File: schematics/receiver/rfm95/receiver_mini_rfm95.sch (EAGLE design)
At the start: 23 parts, among them IC1 ATMEGA328P, Q1 16MHz, Q2 BC817-16SMD, U1 RFM95_LORA_MODULE, U2 AMS1117_3.3

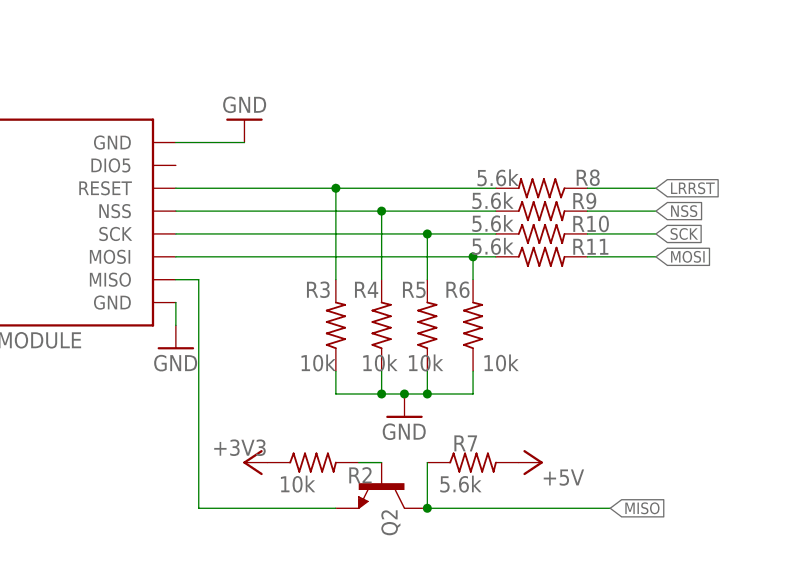
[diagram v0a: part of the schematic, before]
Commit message: Fixed incorrect resistor values
- Fixed incorrect resistor values in the level shifters.
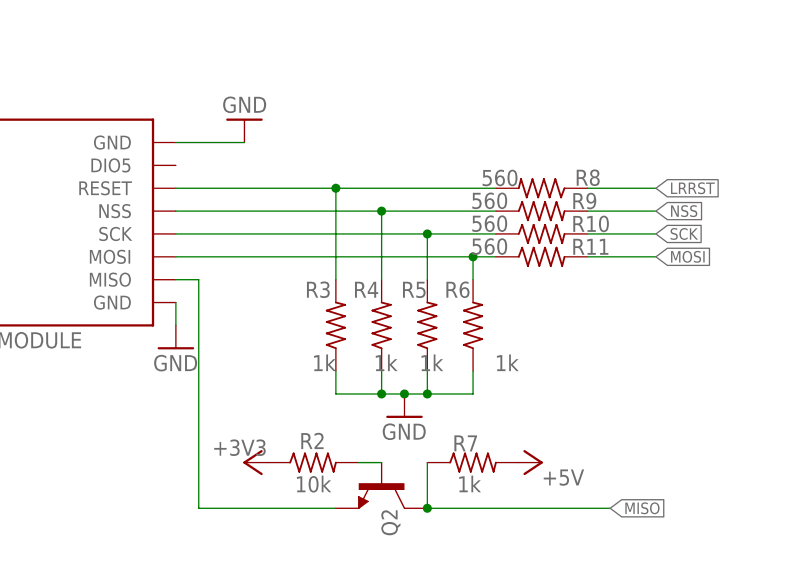
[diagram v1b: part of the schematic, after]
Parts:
- R10, R11, R8, R9: value 5.6k -> 560
- R3, R4, R5, R6: value 10k -> 1k
- R7: value 5.6k -> 1k
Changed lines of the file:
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@@
 <part name="U1" library="RFM95_Lora_module" deviceset="RFM95_LORA_MODULE" device=""/>
 <part name="Q2" library="transistor-npn" deviceset="BC817*" device="SMD" technology="-16" value=""/>
-<part name="R7" library="rcl" deviceset="R-US_" device="R0805" value="5.6k"/>
+<part name="R7" library="rcl" deviceset="R-US_" device="R0805" value="1k"/>
 <part name="R2" library="rcl" deviceset="R-US_" device="R0805" value="10k"/>
 <part name="+3V32" library="supply1" deviceset="+3V3" device=""/>
@@
 <part name="R12" library="rcl" deviceset="R-US_" device="R0805" value="1k"/>
 <part name="P+4" library="supply1" deviceset="+5V" device=""/>
-<part name="R9" library="rcl" deviceset="R-US_" device="R0805" value="5.6k"/>
-<part name="R5" library="rcl" deviceset="R-US_" device="R0805" value="10k"/>
-<part name="R8" library="rcl" deviceset="R-US_" device="R0805" value="5.6k"/>
-<part name="R4" library="rcl" deviceset="R-US_" device="R0805" value="10k"/>
-<part name="R10" library="rcl" deviceset="R-US_" device="R0805" value="5.6k"/>
-<part name="R3" library="rcl" deviceset="R-US_" device="R0805" value="10k"/>
-<part name="R11" library="rcl" deviceset="R-US_" device="R0805" value="5.6k"/>
-<part name="R6" library="rcl" deviceset="R-US_" device="R0805" value="10k"/>
+<part name="R9" library="rcl" deviceset="R-US_" device="R0805" value="560"/>
+<part name="R5" library="rcl" deviceset="R-US_" device="R0805" value="1k"/>
+<part name="R8" library="rcl" deviceset="R-US_" device="R0805" value="560"/>
+<part name="R4" library="rcl" deviceset="R-US_" device="R0805" value="1k"/>
+<part name="R10" library="rcl" deviceset="R-US_" device="R0805" value="560"/>
+<part name="R3" library="rcl" deviceset="R-US_" device="R0805" value="1k"/>
+<part name="R11" library="rcl" deviceset="R-US_" device="R0805" value="560"/>
+<part name="R6" library="rcl" deviceset="R-US_" device="R0805" value="1k"/>
 <part name="GND7" library="supply1" deviceset="GND" device=""/>
 <part name="P+2" library="supply1" deviceset="+5V" device=""/>
@@
 <instance part="R7" gate="G$1" x="119.38" y="-33.02" smashed="yes">
 <attribute name="NAME" x="117.094" y="-31.7754" size="1.778" layer="95"/>
-<attribute name="VALUE" x="115.57" y="-36.322" size="1.778" layer="96"/>
+<attribute name="VALUE" x="117.602" y="-36.322" size="1.778" layer="96"/>
 </instance>
 <instance part="R2" gate="G$1" x="101.6" y="-33.02" smashed="yes">
-<attribute name="NAME" x="105.41" y="-35.3314" size="1.778" layer="95"/>
-<attribute name="VALUE" x="97.79" y="-36.322" size="1.778" layer="96"/>
+<attribute name="NAME" x="100.076" y="-31.5214" size="1.778" layer="95"/>
+<attribute name="VALUE" x="99.568" y="-36.322" size="1.778" layer="96"/>
 </instance>
 <instance part="+3V32" gate="G$1" x="93.98" y="-33.02" smashed="yes" rot="R90">
